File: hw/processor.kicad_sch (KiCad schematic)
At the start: 2 parts, among them U1 ISP2454-LP-JT

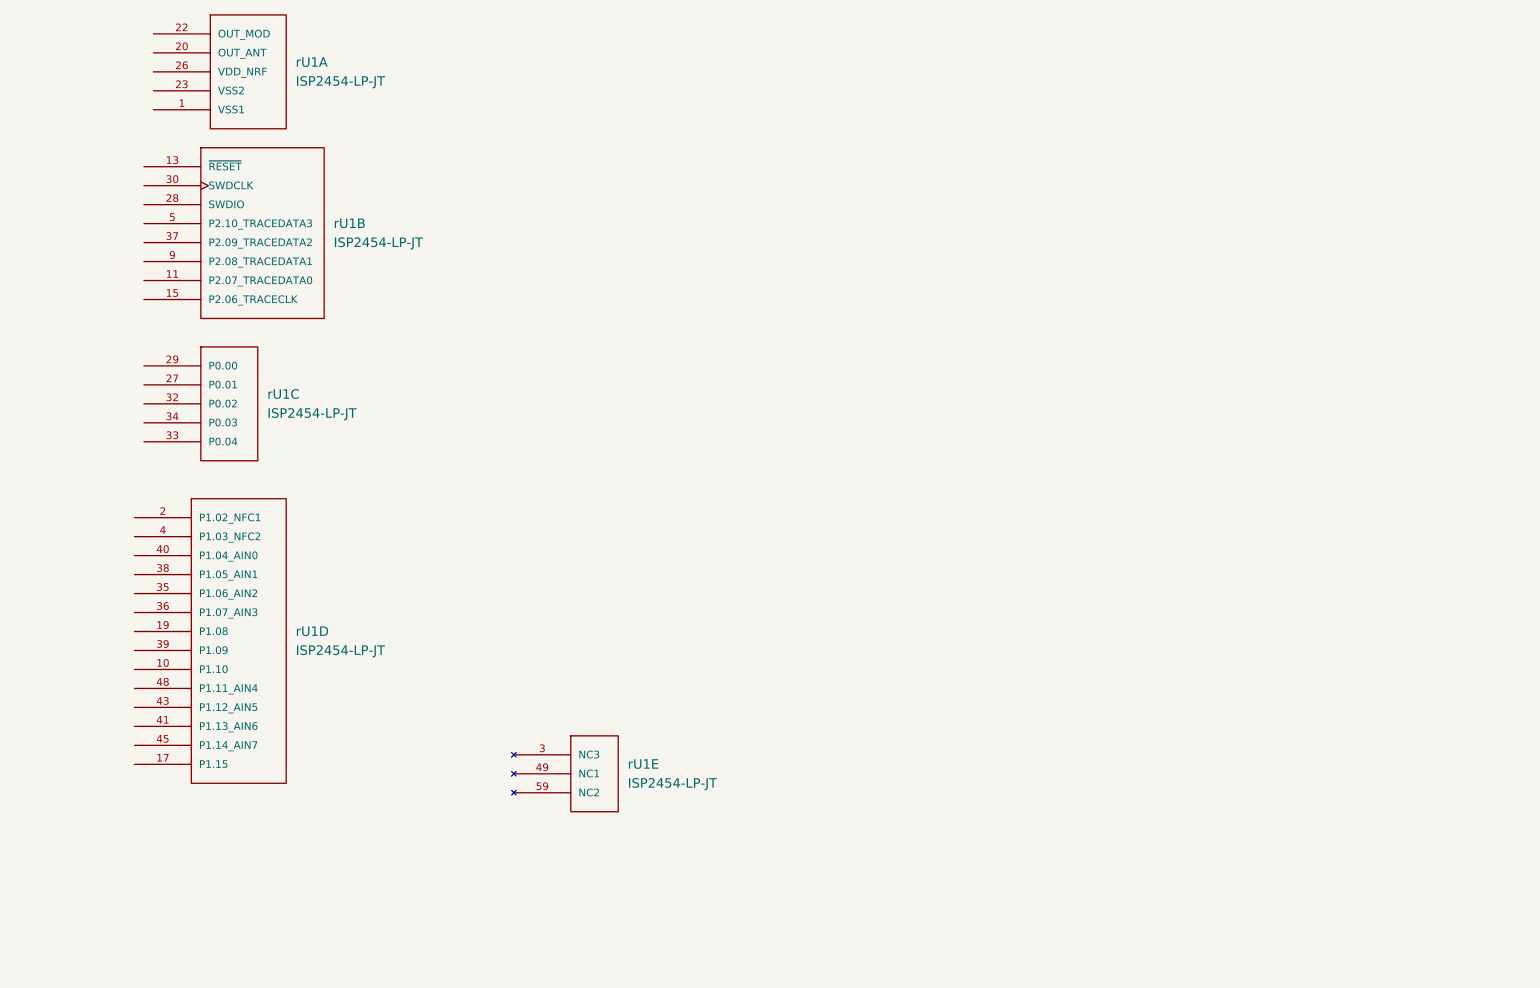
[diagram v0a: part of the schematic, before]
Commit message: Power schematic with npm1100 setup
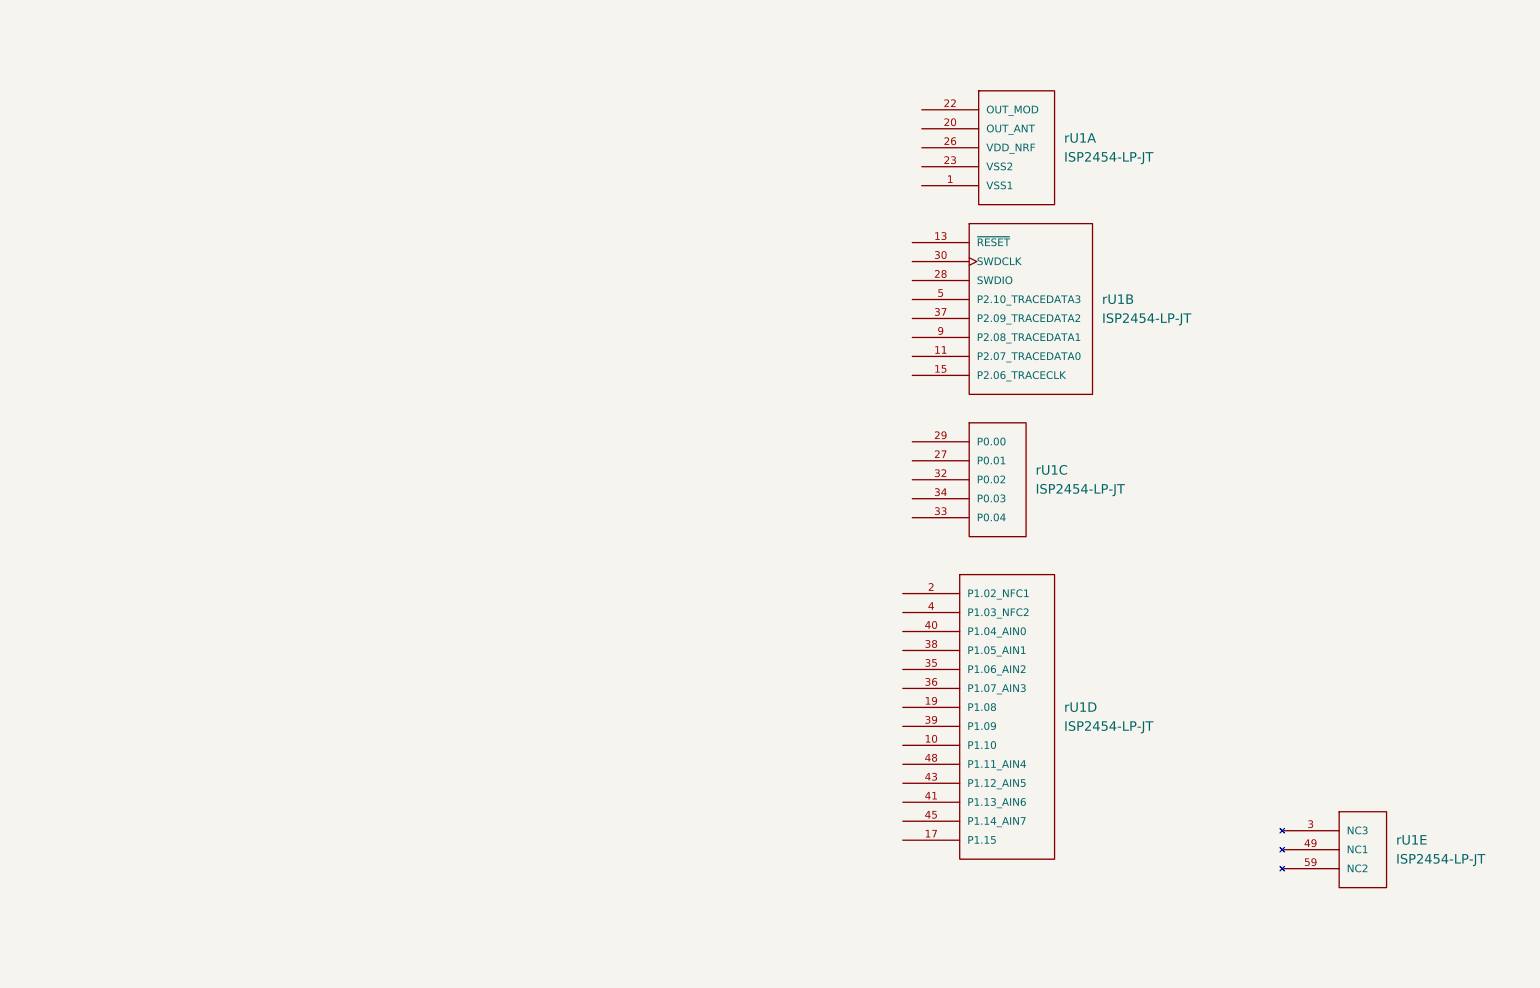
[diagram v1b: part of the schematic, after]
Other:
- moved on the sheet: rU1A, rU1B, rU1C, rU1D, rU1E
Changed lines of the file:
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@@
 	(generator "eeschema")
 	(generator_version "9.0")
-	(paper "A4")
+	(paper "A3")
 	(symbol
 		(lib_id "Alidade:ISP2454-LP-JT")
-		(at 186.69 45.72 0)
+		(at 289.56 55.88 0)
 		(unit 1)
 		(exclude_from_sim no)
@@
 		(fields_autoplaced yes)
 		(property "Reference" "rU1"
-			(at 205.74 52.0699 0)
+			(at 308.61 62.2299 0)
 			(effects
 				(font
@@
 		)
 		(property "Value" "ISP2454-LP-JT"
-			(at 205.74 54.6099 0)
+			(at 308.61 64.7699 0)
 			(effects
 				(font
@@
 		)
 		(property "Footprint" "Alidade:XCVR_ISP2454-LX-JT"
-			(at 201.168 36.576 0)
+			(at 304.038 46.736 0)
 			(effects
 				(font
@@
 		)
 		(property "Datasheet" ""
-			(at 186.69 45.72 0)
+			(at 289.56 55.88 0)
 			(effects
 				(font
@@
 		)
 		(property "Description" ""
-			(at 186.69 45.72 0)
+			(at 289.56 55.88 0)
 			(effects
 				(font
@@
 	(symbol
 		(lib_id "Alidade:ISP2454-LP-JT")
-		(at 184.15 110.49 0)
+		(at 287.02 120.65 0)
 		(unit 4)
 		(exclude_from_sim no)
@@
 		(fields_autoplaced yes)
 		(property "Reference" "rU1"
-			(at 205.74 128.2699 0)
+			(at 308.61 138.4299 0)
 			(effects
 				(font
@@
 		)
 		(property "Value" "ISP2454-LP-JT"
-			(at 205.74 130.8099 0)
+			(at 308.61 140.9699 0)
 			(effects
 				(font
@@
 		)
 		(property "Footprint" "Alidade:XCVR_ISP2454-LX-JT"
-			(at 198.628 101.346 0)
+			(at 301.498 111.506 0)
 			(effects
 				(font
@@
 		)
 		(property "Datasheet" ""
-			(at 184.15 110.49 0)
+			(at 287.02 120.65 0)
 			(effects
 				(font
@@
 		)
 		(property "Description" ""
-			(at 184.15 110.49 0)
+			(at 287.02 120.65 0)
 			(effects
 				(font
@@
 	(symbol
 		(lib_id "Alidade:ISP2454-LP-JT")
-		(at 185.42 63.5 0)
+		(at 288.29 73.66 0)
 		(unit 2)
 		(exclude_from_sim no)
@@
 		(fields_autoplaced yes)
 		(property "Reference" "rU1"
-			(at 210.82 73.6599 0)
+			(at 313.69 83.8199 0)
 			(effects
 				(font
@@
 		)
 		(property "Value" "ISP2454-LP-JT"
-			(at 210.82 76.1999 0)
+			(at 313.69 86.3599 0)
 			(effects
 				(font
@@
 		)
 		(property "Footprint" "Alidade:XCVR_ISP2454-LX-JT"
-			(at 199.898 54.356 0)
+			(at 302.768 64.516 0)
 			(effects
 				(font
@@
 		)
 		(property "Datasheet" ""
-			(at 185.42 63.5 0)
+			(at 288.29 73.66 0)
 			(effects
 				(font
@@
 		)
 		(property "Description" ""
-			(at 185.42 63.5 0)
+			(at 288.29 73.66 0)
 			(effects
 				(font
@@
 	(symbol
 		(lib_id "Alidade:ISP2454-LP-JT")
-		(at 234.95 142.24 0)
+		(at 337.82 152.4 0)
 		(unit 5)
 		(exclude_from_sim no)
@@
 		(fields_autoplaced yes)
 		(property "Reference" "rU1"
-			(at 250.19 146.0499 0)
+			(at 353.06 156.2099 0)
 			(effects
 				(font
@@
 		)
 		(property "Value" "ISP2454-LP-JT"
-			(at 250.19 148.5899 0)
+			(at 353.06 158.7499 0)
 			(effects
 				(font
@@
 		)
 		(property "Footprint" "Alidade:XCVR_ISP2454-LX-JT"
-			(at 249.428 133.096 0)
+			(at 352.298 143.256 0)
 			(effects
 				(font
@@
 		)
 		(property "Datasheet" ""
-			(at 234.95 142.24 0)
+			(at 337.82 152.4 0)
 			(effects
 				(font
@@
 		)
 		(property "Description" ""
-			(at 234.95 142.24 0)
+			(at 337.82 152.4 0)
 			(effects
 				(font
@@
 	(symbol
 		(lib_id "Alidade:ISP2454-LP-JT")
-		(at 185.42 90.17 0)
+		(at 288.29 100.33 0)
 		(unit 3)
 		(exclude_from_sim no)
@@
 		(fields_autoplaced yes)
 		(property "Reference" "rU1"
-			(at 201.93 96.5199 0)
+			(at 304.8 106.6799 0)
 			(effects
 				(font
@@
 		)
 		(property "Value" "ISP2454-LP-JT"
-			(at 201.93 99.0599 0)
+			(at 304.8 109.2199 0)
 			(effects
 				(font
@@
 		)
 		(property "Footprint" "Alidade:XCVR_ISP2454-LX-JT"
-			(at 199.898 81.026 0)
+			(at 302.768 91.186 0)
 			(effects
 				(font
@@
 		)
 		(property "Datasheet" ""
-			(at 185.42 90.17 0)
+			(at 288.29 100.33 0)
 			(effects
 				(font
@@
 		)
 		(property "Description" ""
-			(at 185.42 90.17 0)
-			(effects
-				(font
+			(at 288.29 100.33 0)
+			(effects
+				(font

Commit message: Add sheet pins
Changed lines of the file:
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@@
 	(generator_version "9.0")
 	(paper "A3")
+	(hierarchical_label "ISET"
+		(shape input)
+		(at 63.5 203.2 180)
+		(effects
+			(font
+				(size 1.27 1.27)
+			)
+			(justify right)
+		)
+	)
+	(hierarchical_label "rMODE"
+		(shape input)
+		(at 302.26 200.66 180)
+		(effects
+			(font
+				(size 1.27 1.27)
+			)
+			(justify right)
+		)
+	)
+	(hierarchical_label "rCHG"
+		(shape input)
+		(at 302.26 195.58 180)
+		(effects
+			(font
+				(size 1.27 1.27)
+			)
+			(justify right)
+		)
+	)
+	(hierarchical_label "rERR"
+		(shape input)
+		(at 302.26 193.04 180)
+		(effects
+			(font
+				(size 1.27 1.27)
+			)
+			(justify right)
+		)
+	)
+	(hierarchical_label "MODE"
+		(shape input)
+		(at 63.5 205.74 180)
+		(effects
+			(font
+				(size 1.27 1.27)
+			)
+			(justify right)
+		)
+	)
+	(hierarchical_label "ERR"
+		(shape input)
+		(at 63.5 198.12 180)
+		(effects
+			(font
+				(size 1.27 1.27)
+			)
+			(justify right)
+		)
+	)
+	(hierarchical_label "SHPACT"
+		(shape input)
+		(at 63.5 208.28 180)
+		(effects
+			(font
+				(size 1.27 1.27)
+			)
+			(justify right)
+		)
+	)
+	(hierarchical_label "rISET"
+		(shape input)
+		(at 302.26 198.12 180)
+		(effects
+			(font
+				(size 1.27 1.27)
+			)
+			(justify right)
+		)
+	)
+	(hierarchical_label "rSHPACT"
+		(shape input)
+		(at 302.26 203.2 180)
+		(effects
+			(font
+				(size 1.27 1.27)
+			)
+			(justify right)
+		)
+	)
+	(hierarchical_label "CHG"
+		(shape input)
+		(at 63.5 200.66 180)
+		(effects
+			(font
+				(size 1.27 1.27)
+			)
+			(justify right)
+		)
+	)
 	(symbol
 		(lib_id "Alidade:ISP2454-LP-JT")

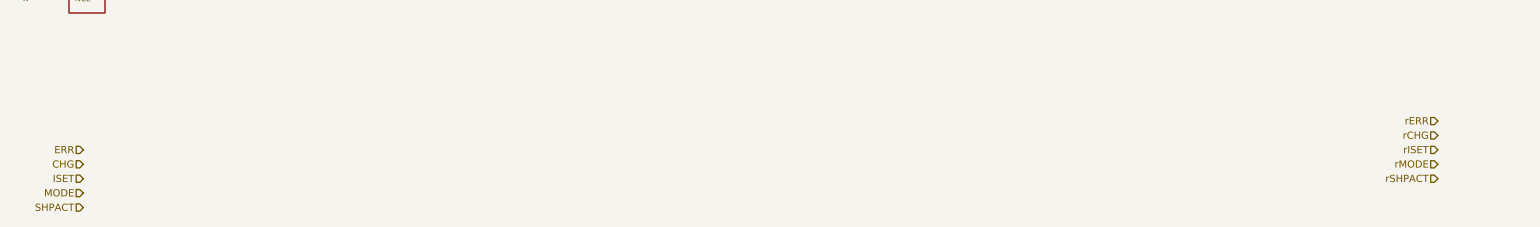
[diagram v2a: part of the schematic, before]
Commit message: Sheet pin directions
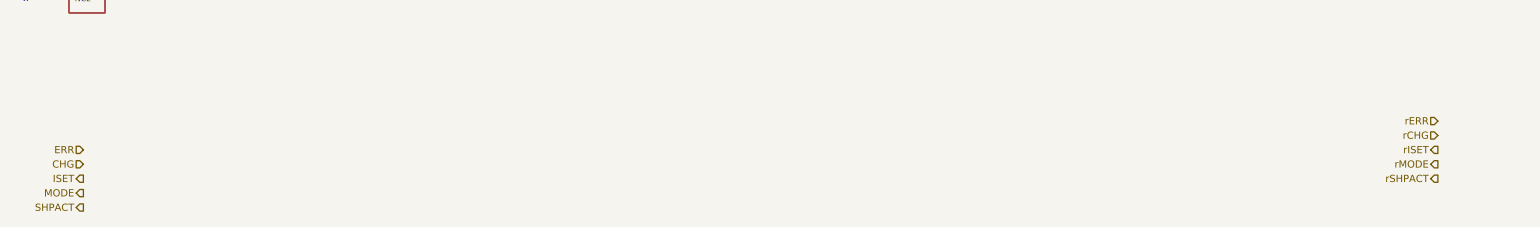
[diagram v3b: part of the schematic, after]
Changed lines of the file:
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@@
 	(paper "A3")
 	(hierarchical_label "ISET"
-		(shape input)
+		(shape output)
 		(at 63.5 203.2 180)
 		(effects
@@
 	)
 	(hierarchical_label "rMODE"
-		(shape input)
+		(shape output)
 		(at 302.26 200.66 180)
 		(effects
@@
 	)
 	(hierarchical_label "MODE"
-		(shape input)
+		(shape output)
 		(at 63.5 205.74 180)
 		(effects
@@
 	)
 	(hierarchical_label "SHPACT"
-		(shape input)
+		(shape output)
 		(at 63.5 208.28 180)
 		(effects
@@
 	)
 	(hierarchical_label "rISET"
-		(shape input)
+		(shape output)
 		(at 302.26 198.12 180)
 		(effects
@@
 	)
 	(hierarchical_label "rSHPACT"
-		(shape input)
+		(shape output)
 		(at 302.26 203.2 180)
 		(effects

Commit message: Battery Monitor
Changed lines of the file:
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@@
+		)
+	)
+	(hierarchical_label "rBATMONEN"
+		(shape output)
+		(at 302.26 208.28 180)
+		(effects
+			(font
+				(size 1.27 1.27)
+			)
+			(justify right)
 		)
 	)
@@
 		)
 	)
+	(hierarchical_label "rBATMON"
+		(shape input)
+		(at 302.26 205.74 180)
+		(effects
+			(font
+				(size 1.27 1.27)
+			)
+			(justify right)
+		)
+	)
 	(hierarchical_label "CHG"
 		(shape input)
@@
 		(effects
 			(font
+				(size 1.27 1.27)
+			)
+			(justify right)
+		)
+	)
+	(hierarchical_label "BATMON"
+		(shape input)
+		(at 63.5 210.82 180)
+		(effects
+			(font
+				(size 1.27 1.27)
+			)
+			(justify right)
+		)
+	)
+	(hierarchical_label "BATMONEN"
+		(shape output)
+		(at 63.5 213.36 180)
+		(effects
+			(font

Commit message: Switch matrix and sheet pins
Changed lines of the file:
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@@
+		)
+	)
+	(hierarchical_label "rCOL4"
+		(shape output)
+		(at 300.99 226.06 90)
+		(effects
+			(font
+				(size 1.27 1.27)
+			)
+			(justify left)
+		)
+	)
+	(hierarchical_label "ROW1"
+		(shape input)
+		(at 60.96 252.73 90)
+		(effects
+			(font
+				(size 1.27 1.27)
+			)
+			(justify left)
+		)
+	)
+	(hierarchical_label "ROW0"
+		(shape input)
+		(at 45.72 252.73 90)
+		(effects
+			(font
+				(size 1.27 1.27)
+			)
+			(justify left)
 		)
 	)
@@
 		)
 	)
+	(hierarchical_label "rROW0"
+		(shape input)
+		(at 297.18 241.3 90)
+		(effects
+			(font
+				(size 1.27 1.27)
+			)
+			(justify left)
+		)
+	)
+	(hierarchical_label "rROW2"
+		(shape input)
+		(at 266.7 241.3 90)
+		(effects
+			(font
+				(size 1.27 1.27)
+			)
+			(justify left)
+		)
+	)
 	(hierarchical_label "MODE"
 		(shape output)
@@
 		)
 	)
+	(hierarchical_label "COL2"
+		(shape output)
+		(at 96.52 238.76 90)
+		(effects
+			(font
+				(size 1.27 1.27)
+			)
+			(justify left)
+		)
+	)
+	(hierarchical_label "COL5"
+		(shape output)
+		(at 58.42 238.76 90)
+		(effects
+			(font
+				(size 1.27 1.27)
+			)
+			(justify left)
+		)
+	)
 	(hierarchical_label "ERR"
 		(shape input)
@@
 		)
 	)
+	(hierarchical_label "COL6"
+		(shape output)
+		(at 45.72 238.76 90)
+		(effects
+			(font
+				(size 1.27 1.27)
+			)
+			(justify left)
+		)
+	)
 	(hierarchical_label "rBATMONEN"
 		(shape output)
@@
 		)
 	)
+	(hierarchical_label "COL1"
+		(shape output)
+		(at 109.22 238.76 90)
+		(effects
+			(font
+				(size 1.27 1.27)
+			)
+			(justify left)
+		)
+	)
+	(hierarchical_label "COL3"
+		(shape output)
+		(at 83.82 238.76 90)
+		(effects
+			(font
+				(size 1.27 1.27)
+			)
+			(justify left)
+		)
+	)
 	(hierarchical_label "rISET"
 		(shape output)
@@
 		)
 	)
+	(hierarchical_label "rROW3"
+		(shape input)
+		(at 251.46 241.3 90)
+		(effects
+			(font
+				(size 1.27 1.27)
+			)
+			(justify left)
+		)
+	)
+	(hierarchical_label "rCOL6"
+		(shape output)
+		(at 326.39 226.06 90)
+		(effects
+			(font
+				(size 1.27 1.27)
+			)
+			(justify left)
+		)
+	)
+	(hierarchical_label "rCOL0"
+		(shape output)
+		(at 250.19 226.06 90)
+		(effects
+			(font
+				(size 1.27 1.27)
+			)
+			(justify left)
+		)
+	)
+	(hierarchical_label "rCOL5"
+		(shape output)
+		(at 313.69 226.06 90)
+		(effects
+			(font
+				(size 1.27 1.27)
+			)
+			(justify left)
+		)
+	)
+	(hierarchical_label "ROW2"
+		(shape input)
+		(at 76.2 252.73 90)
+		(effects
+			(font
+				(size 1.27 1.27)
+			)
+			(justify left)
+		)
+	)
+	(hierarchical_label "ROW3"
+		(shape input)
+		(at 91.44 252.73 90)
+		(effects
+			(font
+				(size 1.27 1.27)
+			)
+			(justify left)
+		)
+	)
+	(hierarchical_label "rCOL1"
+		(shape output)
+		(at 262.89 226.06 90)
+		(effects
+			(font
+				(size 1.27 1.27)
+			)
+			(justify left)
+		)
+	)
 	(hierarchical_label "rSHPACT"
 		(shape output)
@@
 		)
 	)
+	(hierarchical_label "rCOL2"
+		(shape output)
+		(at 275.59 226.06 90)
+		(effects
+			(font
+				(size 1.27 1.27)
+			)
+			(justify left)
+		)
+	)
+	(hierarchical_label "COL4"
+		(shape output)
+		(at 71.12 238.76 90)
+		(effects
+			(font
+				(size 1.27 1.27)
+			)
+			(justify left)
+		)
+	)
 	(hierarchical_label "CHG"
 		(shape input)
@@
 		)
 	)
+	(hierarchical_label "rCOL3"
+		(shape output)
+		(at 288.29 226.06 90)
+		(effects
+			(font
+				(size 1.27 1.27)
+			)
+			(justify left)
+		)
+	)
 	(hierarchical_label "BATMON"
 		(shape input)
@@
 		)
 	)
+	(hierarchical_label "COL0"
+		(shape output)
+		(at 121.92 238.76 90)
+		(effects
+			(font
+				(size 1.27 1.27)
+			)
+			(justify left)
+		)
+	)
 	(hierarchical_label "BATMONEN"
 		(shape output)
@@
 		)
 	)
+	(hierarchical_label "rROW1"
+		(shape input)
+		(at 281.94 241.3 90)
+		(effects
+			(font
+				(size 1.27 1.27)
+			)
+			(justify left)
+		)
+	)

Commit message: Sheet pins
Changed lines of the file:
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@@
 	(generator_version "9.0")
 	(paper "A3")
-	(hierarchical_label "ISET"
-		(shape output)
-		(at 63.5 203.2 180)
-		(effects
-			(font
-				(size 1.27 1.27)
-			)
-			(justify right)
-		)
-	)
-	(hierarchical_label "rMODE"
-		(shape output)
-		(at 302.26 200.66 180)
+	(hierarchical_label "SCL"
+		(shape output)
+		(at 130.81 196.85 180)
 		(effects
 			(font
@@
 		)
 	)
-	(hierarchical_label "rCHG"
-		(shape input)
-		(at 302.26 195.58 180)
-		(effects
-			(font
-				(size 1.27 1.27)
-			)
-			(justify right)
-		)
-	)
-	(hierarchical_label "rERR"
-		(shape input)
-		(at 302.26 193.04 180)
-		(effects
-			(font
-				(size 1.27 1.27)
-			)
-			(justify right)
-		)
-	)
 	(hierarchical_label "rROW0"
 		(shape input)
@@
 		)
 	)
-	(hierarchical_label "MODE"
-		(shape output)
-		(at 63.5 205.74 180)
-		(effects
-			(font
-				(size 1.27 1.27)
-			)
-			(justify right)
-		)
-	)
 	(hierarchical_label "COL2"
 		(shape output)
@@
 		)
 	)
-	(hierarchical_label "ERR"
-		(shape input)
-		(at 63.5 198.12 180)
-		(effects
-			(font
-				(size 1.27 1.27)
-			)
-			(justify right)
-		)
-	)
 	(hierarchical_label "COL6"
 		(shape output)
@@
 		)
 	)
-	(hierarchical_label "rBATMONEN"
-		(shape output)
-		(at 302.26 208.28 180)
-		(effects
-			(font
-				(size 1.27 1.27)
-			)
-			(justify right)
-		)
-	)
-	(hierarchical_label "SHPACT"
-		(shape output)
-		(at 63.5 208.28 180)
-		(effects
-			(font
-				(size 1.27 1.27)
-			)
-			(justify right)
-		)
-	)
 	(hierarchical_label "COL1"
 		(shape output)
@@
 		)
 	)
+	(hierarchical_label "rSCL"
+		(shape output)
+		(at 255.27 157.48 180)
+		(effects
+			(font
+				(size 1.27 1.27)
+			)
+			(justify right)
+		)
+	)
 	(hierarchical_label "COL3"
 		(shape output)
@@
 		)
 	)
-	(hierarchical_label "rISET"
-		(shape output)
-		(at 302.26 198.12 180)
+	(hierarchical_label "rPMICINT"
+		(shape input)
+		(at 256.54 148.59 180)
 		(effects
 			(font
@@
 		)
 	)
+	(hierarchical_label "PMICINT"
+		(shape input)
+		(at 129.54 191.77 180)
+		(effects
+			(font
+				(size 1.27 1.27)
+			)
+			(justify right)
+		)
+	)
 	(hierarchical_label "rCOL0"
 		(shape output)
@@
 		)
 	)
-	(hierarchical_label "rSHPACT"
-		(shape output)
-		(at 302.26 203.2 180)
-		(effects
-			(font
-				(size 1.27 1.27)
-			)
-			(justify right)
-		)
-	)
-	(hierarchical_label "rBATMON"
-		(shape input)
-		(at 302.26 205.74 180)
-		(effects
-			(font
-				(size 1.27 1.27)
-			)
-			(justify right)
-		)
-	)
 	(hierarchical_label "rCOL2"
 		(shape output)
@@
 		)
 	)
-	(hierarchical_label "CHG"
-		(shape input)
-		(at 63.5 200.66 180)
+	(hierarchical_label "rSDA"
+		(shape bidirectional)
+		(at 255.27 154.94 180)
+		(effects
+			(font
+				(size 1.27 1.27)
+			)
+			(justify right)
+		)
+	)
+	(hierarchical_label "SDA"
+		(shape bidirectional)
+		(at 130.81 194.31 180)
 		(effects
 			(font
@@
 		)
 	)
-	(hierarchical_label "BATMON"
-		(shape input)
-		(at 63.5 210.82 180)
-		(effects
-			(font
-				(size 1.27 1.27)
-			)
-			(justify right)
-		)
-	)
 	(hierarchical_label "COL0"
 		(shape output)
@@
 		)
 	)
-	(hierarchical_label "BATMONEN"
-		(shape output)
-		(at 63.5 213.36 180)
-		(effects
-			(font
-				(size 1.27 1.27)
-			)
-			(justify right)
-		)
-	)
